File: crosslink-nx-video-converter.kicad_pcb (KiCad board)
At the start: 2 copper layers, 105.7 x 60 mm, 42 parts, among them J1 DC_SOCKET, J2 031-70526-21, J3 031-70526-21, J4 WE_68715014522_ONE-SIDE, J5 FTSH-105-01-F-DV-K, J6 WE_68715014522_ONE-SIDE, J7 2X05, J8 61300411121, Q6 2N7002, SW1 SW_DIP_x06, U10 AP7330-W5-7, U11 LIFCL-40-9BG256C, U12 MT41K128M16JT-125_K, U15 GS2971A, U16 GS2988, U17 SC18IS602BIPW, U18 W25Q32JVSSIQ, U2 LM339, U3 LM339, U4 NCV51200MNTXG, U5 AP62301WU-7, U6 AP62301WU-7, U7 AP62301WU-7, U8 AP7330-W5-7, U9 AP7330-W5-7, Y1 ABM7_27.000MH_D2Y_T, Y2 OSC40M-3.3_S5

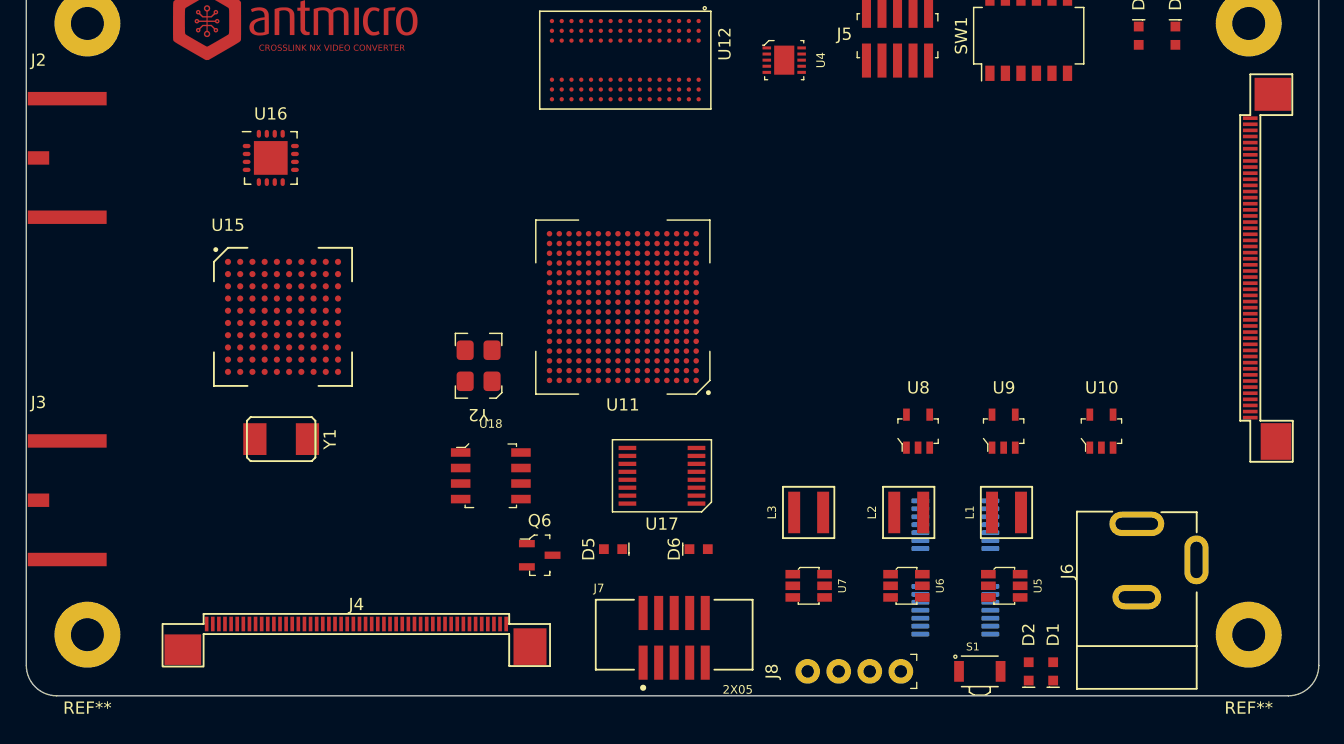
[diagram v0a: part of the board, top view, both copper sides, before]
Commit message: Preliminary FPGA fanout
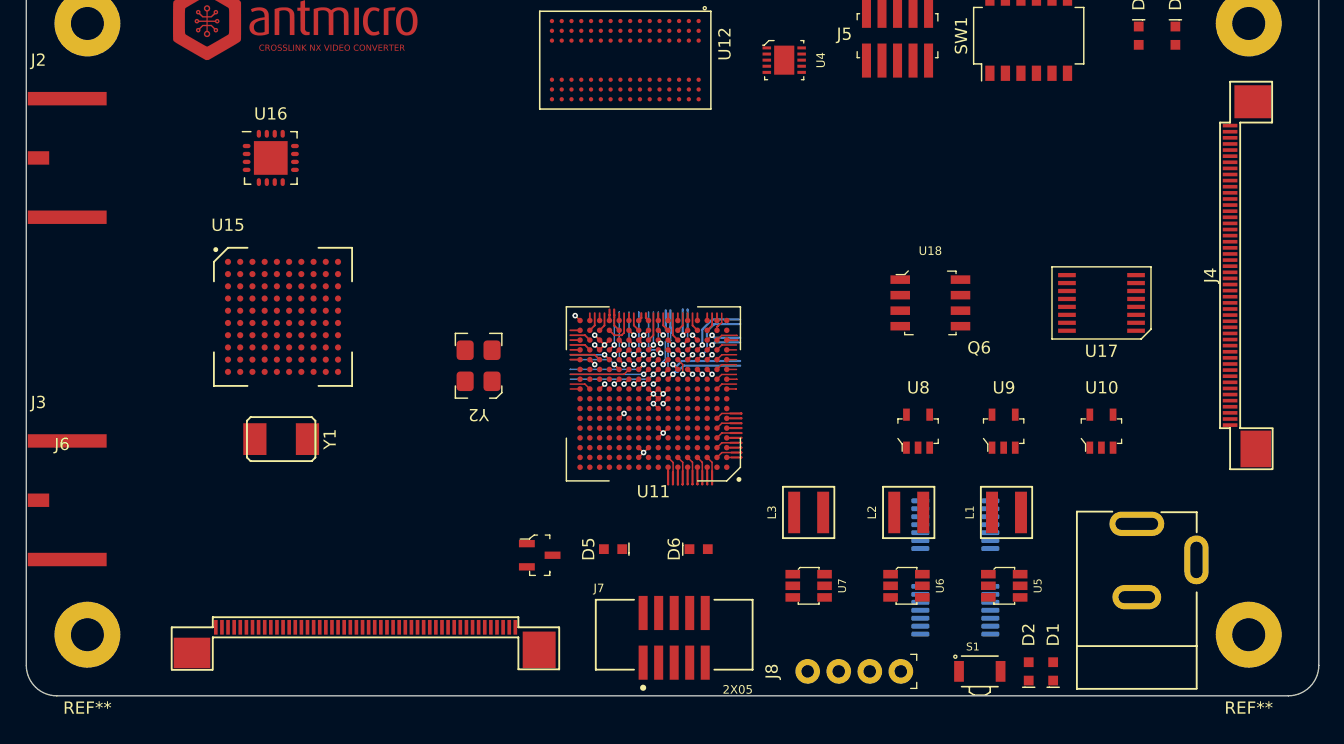
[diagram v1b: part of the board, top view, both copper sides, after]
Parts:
- moved J6 77.3 mm to (102.8, 108.8), turned to 0 degrees
- moved J4 76.2 mm to (172.9, 80.6), turned to 90 degrees
- moved U17 38.6 mm to (163.0, 82.9)
- moved U18 38.6 mm to (149.0, 82.9)
- moved U11 7.53 mm to (126.3, 90.3)
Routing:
- net GND: track 0.00 -> 20.4 mm, vias 0 -> 23
- net /DDR3/DDR3_BA2: track 0.00 -> 7.53 mm, vias 0 -> 1
- net /DDR3/DDR3_A8: track 0.00 -> 6.73 mm, vias 0 -> 1
- net /DDR3/~{DDR3_RAS}: track 0.00 -> 6.57 mm, vias 0 -> 1
- net /Peripherals/MIPI2_D3_N: track 0.00 -> 6.36 mm, vias 0 -> 1
- net /Peripherals/MIPI2_D3_P: track 0.00 -> 6.36 mm, vias 0 -> 1
- net /Peripherals/MIPI2_D2_P: track 0.00 -> 6.19 mm, vias 0 -> 1
- net /Peripherals/MIPI2_D1_N: track 0.00 -> 5.62 mm, vias 0 -> 1
- net /Peripherals/MIPI2_D1_P: track 0.00 -> 5.27 mm, vias 0 -> 1
- net /Peripherals/MIPI2_D2_N: track 0.00 -> 5.24 mm, vias 0 -> 1
- net /DDR3/DDR3_A6: track 0.00 -> 5.03 mm, vias 0 -> 1
- net /DDR3/DDR3_A7: track 0.00 -> 4.97 mm
- net /DDR3/~{DDR3_CAS}: track 0.00 -> 4.42 mm, vias 0 -> 1
- net /DDR3/DDR3_A10: track 0.00 -> 4.33 mm, vias 0 -> 1
- net /DDR3/DDR3_ODT: track 0.00 -> 4.23 mm, vias 0 -> 1
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- added copper zone on In1.Cu, net GND
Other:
- copper layers 2 -> 6

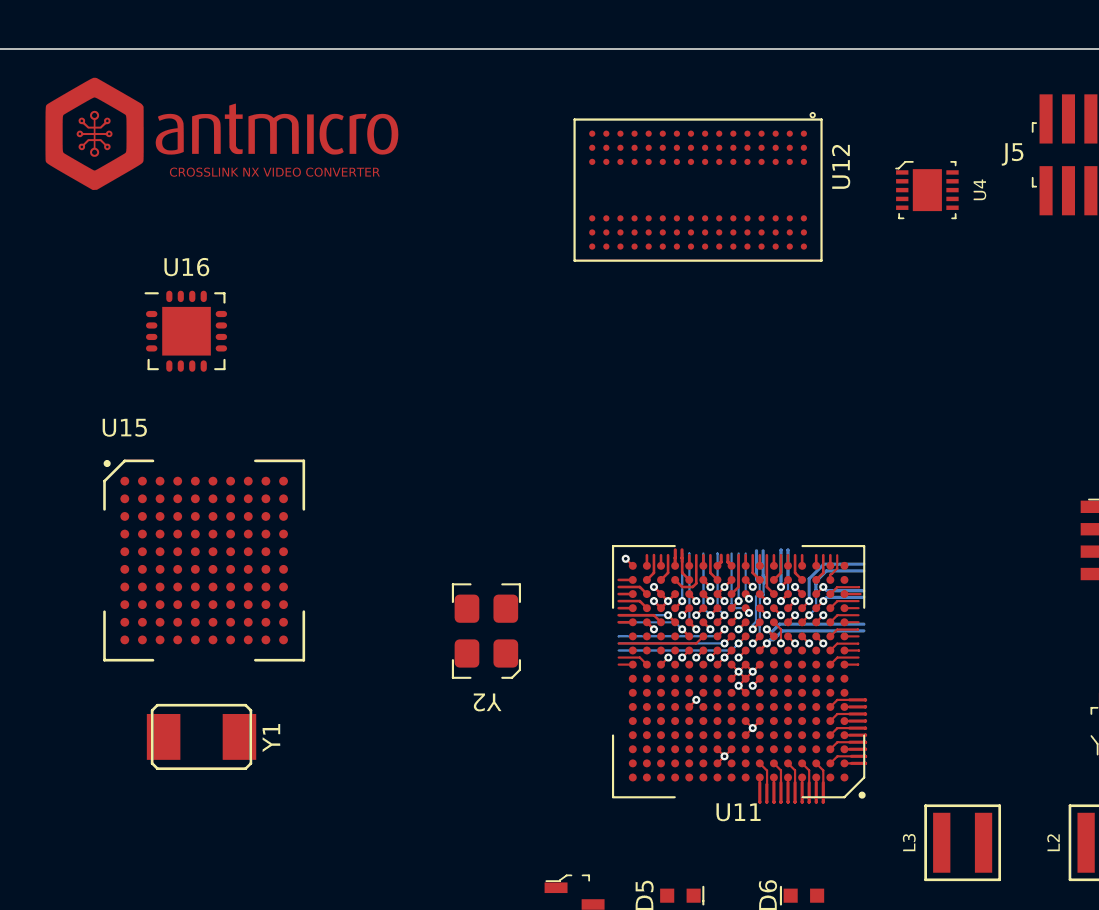
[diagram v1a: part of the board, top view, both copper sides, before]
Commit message: More fanout
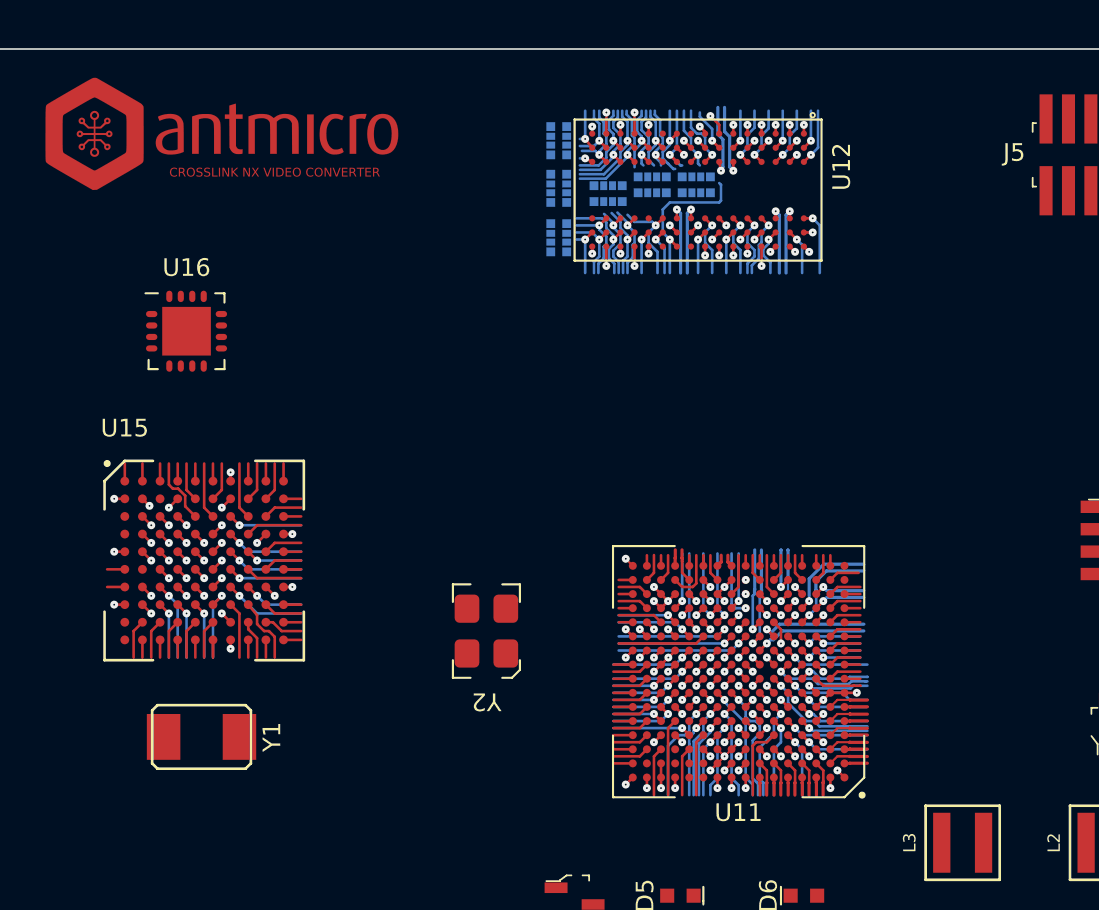
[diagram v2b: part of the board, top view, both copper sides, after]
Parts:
- removed U4: NCV51200MNTXG, crosslink-nx-video-converter-footprints:DFN-10-1EP_3x3mm
- added R44: 4x51R_0402_array, crosslink-nx-video-converter-footprints:R_Array_4x0402, B.Cu at (121.4, 62.7)
- added R45: 4x51R_0402_array, crosslink-nx-video-converter-footprints:R_Array_4x0402, B.Cu at (116.1, 60.2)
- added R46: 4x51R_0402_array, crosslink-nx-video-converter-footprints:R_Array_4x0402, B.Cu at (118.9, 63.2)
- added R48: 4x51R_0402_array, crosslink-nx-video-converter-footprints:R_Array_4x0402, B.Cu at (116.1, 65.7)
- added R49: 4x51R_0402_array, crosslink-nx-video-converter-footprints:R_Array_4x0402, B.Cu at (116.1, 62.9)
- added R50: 4x51R_0402_array, crosslink-nx-video-converter-footprints:R_Array_4x0402, B.Cu at (123.9, 62.7)
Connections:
- J8 pad 2: SCL -> SDA
- J8 pad 3: SDA -> SCL
- U11 pad A14: unconnected-(U11-PadA14) -> GND
- U11 pad A15: unconnected-(U11-PadA15) -> GND
- U11 pad A9: unconnected-(U11-PadA9) -> GND
- U11 pad B9: unconnected-(U11-PadB9) -> GND
- U11 pad C11: unconnected-(U11-PadC11) -> GND
- U11 pad K13: unconnected-(U11-PadK13) -> GND
- U11 pad K14: unconnected-(U11-PadK14) -> GND
- U11 pad K15: unconnected-(U11-PadK15) -> GND
- U11 pad K16: unconnected-(U11-PadK16) -> GND
- U11 pad L13: unconnected-(U11-PadL13) -> GND
- U11 pad L15: unconnected-(U11-PadL15) -> GND
- U11 pad L16: unconnected-(U11-PadL16) -> GND
- U11 pad N6: +1V35 -> +1V5
- U11 pad P11: +1V35 -> +1V5
- U11 pad P12: +1V35 -> +1V5
- U11 pad R2: +1V35 -> +1V5
- U12 pad A1: +1V35 -> +1V5
- U12 pad A8: +1V35 -> +1V5
- U12 pad B2: +1V35 -> +1V5
- U12 pad C1: +1V35 -> +1V5
- U12 pad C9: +1V35 -> +1V5
- U12 pad D2: +1V35 -> +1V5
- U12 pad D9: +1V35 -> +1V5
- U12 pad E9: +1V35 -> +1V5
- U12 pad F1: +1V35 -> +1V5
- U12 pad G7: +1V35 -> +1V5
- U12 pad H2: +1V35 -> +1V5
- U12 pad H9: +1V35 -> +1V5
- U12 pad K2: +1V35 -> +1V5
- U12 pad K8: +1V35 -> +1V5
- U12 pad N1: +1V35 -> +1V5
- U12 pad N9: +1V35 -> +1V5
- U12 pad R1: +1V35 -> +1V5
- U12 pad R9: +1V35 -> +1V5
- U2 pad 10: +1V8 -> /Power Supply/VREF_0V45
- U2 pad 11: /Power Supply/VREF_0V45 -> +1V8
- U2 pad 4: +3V3 -> /Power Supply/VREF_0V45
- U2 pad 5: /Power Supply/VREF_0V45 -> +3V3
- U2 pad 6: 1V0_Power -> /Power Supply/VREF_0V45
- U2 pad 7: /Power Supply/VREF_0V45 -> 1V0_Power
- U2 pad 8: 1V0_Clean -> /Power Supply/VREF_0V45
- U2 pad 9: /Power Supply/VREF_0V45 -> 1V0_Clean
- U3 pad 10: +5V -> GND
- U3 pad 11: /Power Supply/VREF_0V45 -> +5V
- U3 pad 4: +1V35 -> /Power Supply/VREF_0V45
- U3 pad 5: /Power Supply/VREF_0V45 -> +1V5
- U3 pad 6: +1V2 -> /Power Supply/VREF_0V45
- U3 pad 7: /Power Supply/VREF_0V45 -> +1V2
- U3 pad 8: /Power Supply/Vtt_PGOOD -> /Power Supply/VREF_0V45
- U3 pad 9: /Power Supply/VREF_0V45 -> Vtt
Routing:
- net GND: track 20.4 -> 63.0 mm, vias 23 -> 98
- net +1V5: track 0.00 -> 15.9 mm, vias 0 -> 21
- net /SDI/AUDIO_EN/~{DIS}: track 0.00 -> 9.28 mm, vias 0 -> 2
- net /SDI/SDIN_TDI: track 0.00 -> 8.95 mm, vias 0 -> 2
- net /DDR3/DDR3_CKE: track 2.37 -> 11.2 mm, vias 0 -> 1
- net /SDI/SW_EN: track 0.00 -> 8.66 mm, vias 0 -> 1
- net /SDI/SDO_EN/DIS: track 0.00 -> 8.64 mm, vias 0 -> 1
- net /SDI/~{RC_BYP}: track 0.57 -> 9.05 mm, vias 1 -> 2
- net /SDI/SDOUT_TDO: track 0.00 -> 8.45 mm, vias 0 -> 2
- net /SDI/IOPROC_EN/~{DIS}: track 0.00 -> 8.39 mm, vias 0 -> 1
- net /SDI/RESET_TRST: track 0.00 -> 8.24 mm, vias 0 -> 2
- net /SDI/DVB_ASI: track 0.00 -> 8.19 mm, vias 0 -> 2
- net /SDI/JTAG/~{HOST}: track 0.57 -> 8.73 mm
- net /SDI/~{CS_TMS}: track 0.00 -> 8.13 mm, vias 0 -> 2
- net /SDI/SCLK_TCK: track 0.00 -> 8.04 mm, vias 0 -> 1
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
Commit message: Placed components
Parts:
- added C1: C_100n_0402, antmicro-footprints:0402-cap, B.Cu at (144.2, 118.1)
- added C10: C_10u_0603, crosslink-nx-video-converter-footprints:0603-cap, F.Cu at (153.7, 106.7)
- added C100: C_100n_0402, antmicro-footprints:0402-cap, B.Cu at (134.9, 90.5)
- added C101: C_100n_0402, antmicro-footprints:0402-cap, B.Cu at (129.7, 99.4)
- added C102: C_100n_0402, antmicro-footprints:0402-cap, B.Cu at (134.5, 94.5)
- added C103: C_100n_0402, antmicro-footprints:0402-cap, B.Cu at (132.9, 98.2)
- added C104: C_100n_0402, antmicro-footprints:0402-cap, B.Cu at (126.5, 98.8)
- added C105: C_100n_0402, antmicro-footprints:0402-cap, B.Cu at (127.8, 82.1)
- added C106: C_100n_0402, antmicro-footprints:0402-cap, B.Cu at (126.8, 82.1)
- added C107: C_100n_0402, antmicro-footprints:0402-cap, B.Cu at (125.8, 82.1)
- added C11: C_10u_0603, crosslink-nx-video-converter-footprints:0603-cap, F.Cu at (155.1, 99.1)
- added C12: C_10u_0603, crosslink-nx-video-converter-footprints:0603-cap, F.Cu at (164.4, 104.8)
- added C13: C_10u_0603, crosslink-nx-video-converter-footprints:0603-cap, F.Cu at (154.6, 110.2)
- added C14: C_100n_0402, antmicro-footprints:0402-cap, F.Cu at (166.7, 99.8)
- added C15: C_100n_0402, antmicro-footprints:0402-cap, F.Cu at (149.5, 107.9)
- added C16: C_100n_0402, antmicro-footprints:0402-cap, B.Cu at (118.2, 83.0)
- added C17: C_1u_0603, crosslink-nx-video-converter-footprints:0603-cap, F.Cu at (142.7, 114.0)
- added C18: C_1u_0603, crosslink-nx-video-converter-footprints:0603-cap, F.Cu at (135.5, 114.8)
- added C19: C_1u_0603, crosslink-nx-video-converter-footprints:0603-cap, F.Cu at (139.3, 113.5)
- added C2: C_100n_0402, antmicro-footprints:0402-cap, B.Cu at (138.0, 111.2)
- added C20: C_22u_0603, antmicro-footprints:0603-cap, F.Cu at (149.8, 102.5)
- added C21: C_22u_0603, antmicro-footprints:0603-cap, F.Cu at (161.0, 99.5)
- added C22: C_22u_0603, antmicro-footprints:0603-cap, F.Cu at (149.2, 113.6)
- added C23: C_22u_0603, antmicro-footprints:0603-cap, F.Cu at (149.8, 104.1)
- added C24: C_22u_0603, antmicro-footprints:0603-cap, F.Cu at (159.4, 99.5)
- added C25: C_22u_0603, antmicro-footprints:0603-cap, F.Cu at (149.2, 115.2)
- added C26: C_22u_0603, antmicro-footprints:0603-cap, F.Cu at (152.3, 102.5)
- added C27: C_22u_0603, antmicro-footprints:0603-cap, F.Cu at (161.0, 102.1)
- added C28: C_22u_0603, antmicro-footprints:0603-cap, F.Cu at (151.8, 115.2)
- added C29: C_1u_0603, crosslink-nx-video-converter-footprints:0603-cap, F.Cu at (144.2, 106.6)
- added C3: C_100n_0402, antmicro-footprints:0402-cap, F.Cu at (149.8, 71.1)
- added C30: C_1u_0603, crosslink-nx-video-converter-footprints:0603-cap, F.Cu at (134.0, 106.8)
- added C31: C_10u_0603, crosslink-nx-video-converter-footprints:0603-cap, F.Cu at (137.8, 105.5)
- added C32: C_22u_0603, antmicro-footprints:0603-cap, F.Cu at (152.3, 104.1)
- added C33: C_22u_0603, antmicro-footprints:0603-cap, F.Cu at (159.4, 102.1)
- added C34: C_22u_0603, antmicro-footprints:0603-cap, F.Cu at (151.8, 113.6)
- added C35: C_100n_0402, antmicro-footprints:0402-cap, B.Cu at (134.4, 82.8)
- added C36: C_100n_0402, antmicro-footprints:0402-cap, F.Cu at (121.0, 37.1)
- added C37: C_100n_0402, antmicro-footprints:0402-cap, F.Cu at (128.1, 37.1)
- added C38: C_100n_0402, antmicro-footprints:0402-cap, F.Cu at (121.0, 39.6)
- added C39: C_100n_0402, antmicro-footprints:0402-cap, F.Cu at (124.5, 39.6)
- added C4: C_1u_0603, crosslink-nx-video-converter-footprints:0603-cap, F.Cu at (147.1, 68.8)
- added C40: C_100n_0402, antmicro-footprints:0402-cap, F.Cu at (135.3, 89.0)
- added C41: C_100n_0402, crosslink-nx-video-converter-footprints:0402-cap, F.Cu at (133.6, 38.9)
- added C42: C_100n_0402, crosslink-nx-video-converter-footprints:0402-cap, F.Cu at (120.6, 44.3)
- added C43: C_100n_0402, crosslink-nx-video-converter-footprints:0402-cap, F.Cu at (134.2, 36.9)
- added C44: C_100n_0402, crosslink-nx-video-converter-footprints:0402-cap, F.Cu at (130.0, 41.3)
- added C45: C_100n_0402, crosslink-nx-video-converter-footprints:0402-cap, F.Cu at (127.7, 39.4)
- added C46: C_100n_0402, crosslink-nx-video-converter-footprints:0402-cap, F.Cu at (124.2, 41.8)
- added C47: C_100n_0402, crosslink-nx-video-converter-footprints:0402-cap, F.Cu at (124.2, 43.8)
- added C48: C_100n_0402, crosslink-nx-video-converter-footprints:0402-cap, F.Cu at (130.6, 39.4)
- added C49: C_100n_0402, crosslink-nx-video-converter-footprints:0402-cap, F.Cu at (131.3, 36.9)
- added C5: C_22u_0603, antmicro-footprints:0603-cap, F.Cu at (144.9, 74.0)
- added C50: C_100n_0402, crosslink-nx-video-converter-footprints:0402-cap, F.Cu at (127.1, 43.8)
- added C51: C_33p_0402, antmicro-footprints:0402-cap, F.Cu at (100.4, 87.8)
- added C52: C_33p_0402, antmicro-footprints:0402-cap, F.Cu at (92.8, 87.8)
- added C53: C_1u_0402, crosslink-nx-video-converter-footprints:0402-cap, F.Cu at (79.3, 38.8)
- added C54: C_1u_0402, crosslink-nx-video-converter-footprints:0402-cap, F.Cu at (75.8, 43.3)
- added C55: C_47n_0603, crosslink-nx-video-converter-footprints:0603-cap, F.Cu at (65.4, 34.1)
- added C56: C_470n_0603, crosslink-nx-video-converter-footprints:0603-cap, F.Cu at (61.9, 34.1)
- added C57: C_1u_0402, crosslink-nx-video-converter-footprints:0402-cap, F.Cu at (82.9, 33.9)
- added C58: C_100n_0402, antmicro-footprints:0402-cap, B.Cu at (117.8, 94.8)
- added C59: C_470n_0603, crosslink-nx-video-converter-footprints:0603-cap, F.Cu at (76.1, 34.1)
- added C6: C_100n_0402, antmicro-footprints:0402-cap, F.Cu at (147.2, 73.7)
- added C60: C_100n_0402, antmicro-footprints:0402-cap, F.Cu at (69.0, 39.1)
- added C61: C_100n_0402, antmicro-footprints:0402-cap, F.Cu at (65.4, 39.1)
- added C62: C_100n_0402, antmicro-footprints:0402-cap, F.Cu at (61.9, 41.5)
- added C63: C_100n_0402, antmicro-footprints:0402-cap, F.Cu at (79.6, 34.1)
- added C64: C_100n_0402, antmicro-footprints:0402-cap, F.Cu at (69.0, 44.0)
- added C65: C_100n_0402, antmicro-footprints:0402-cap, B.Cu at (117.8, 93.8)
- added C66: C_100n_0402, antmicro-footprints:0402-cap, F.Cu at (65.4, 36.6)
- added C67: C_100n_0402, antmicro-footprints:0402-cap, F.Cu at (61.9, 44.0)
- added C68: C_100n_0402, antmicro-footprints:0402-cap, F.Cu at (72.5, 34.1)
- added C69: C_100n_0402, antmicro-footprints:0402-cap, F.Cu at (72.5, 39.1)
- added C7: C_22u_0603, antmicro-footprints:0603-cap, F.Cu at (141.8, 70.3)
- added C70: C_100n_0402, antmicro-footprints:0402-cap, F.Cu at (61.9, 36.6)
- added C71: C_33u_0603, crosslink-nx-video-converter-footprints:0603-cap, F.Cu at (65.4, 46.5)
- added C72: C_100n_0402, antmicro-footprints:0402-cap, F.Cu at (61.9, 46.5)
- added C73: C_100n_0402, antmicro-footprints:0402-cap, F.Cu at (65.4, 44.0)
- added C74: C_100n_0402, antmicro-footprints:0402-cap, F.Cu at (65.4, 41.5)
- added C75: C_100n_0402, antmicro-footprints:0402-cap, F.Cu at (69.0, 34.1)
- added C76: C_10n_0402, crosslink-nx-video-converter-footprints:0402-cap, F.Cu at (68.7, 48.2)
- added C77: C_4u7_0402, crosslink-nx-video-converter-footprints:0402-cap, F.Cu at (75.8, 41.3)
- added C78: C_4u7_0402, crosslink-nx-video-converter-footprints:0402-cap, F.Cu at (72.2, 45.8)
- added C79: C_100n_0402, antmicro-footprints:0402-cap, F.Cu at (115.8, 88.8)
- added C8: C_22u_0603, antmicro-footprints:0603-cap, F.Cu at (140.2, 70.3)
- added C80: C_100n_0402, antmicro-footprints:0402-cap, F.Cu at (152.0, 118.0)
- added C81: C_100n_0402, antmicro-footprints:0402-cap, B.Cu at (158.2, 71.2)
- added C82: C_100n_0402, antmicro-footprints:0402-cap, B.Cu at (105.6, 95.2)
- added C83: C_100n_0402, antmicro-footprints:0402-cap, B.Cu at (135.1, 86.9)
- added C84: C_100n_0402, antmicro-footprints:0402-cap, F.Cu at (135.3, 88.0)
- added C85: C_100n_0402, antmicro-footprints:0402-cap, B.Cu at (124.5, 98.8)
- added C86: C_10u_0603, crosslink-nx-video-converter-footprints:0603-cap, F.Cu at (214.2, 111.4)
- added C87: C_10u_0603, crosslink-nx-video-converter-footprints:0603-cap, F.Cu at (200.0, 111.4)
- added C88: C_10u_0603, crosslink-nx-video-converter-footprints:0603-cap, F.Cu at (200.0, 118.8)
- added C89: C_10u_0603, crosslink-nx-video-converter-footprints:0603-cap, F.Cu at (207.1, 113.9)
- added C9: C_100n_0402, antmicro-footprints:0402-cap, F.Cu at (150.1, 96.8)
- added C90: C_10u_0603, crosslink-nx-video-converter-footprints:0603-cap, F.Cu at (203.6, 118.8)
- added C91: C_1u_0603, crosslink-nx-video-converter-footprints:0603-cap, F.Cu at (217.8, 113.9)
- added C92: C_10u_0603, crosslink-nx-video-converter-footprints:0603-cap, F.Cu at (203.6, 121.3)
- added C93: C_100n_0402, antmicro-footprints:0402-cap, B.Cu at (129.8, 82.1)
- added C94: C_100n_0402, antmicro-footprints:0402-cap, B.Cu at (134.9, 91.5)
- added C95: C_100n_0402, antmicro-footprints:0402-cap, B.Cu at (127.5, 99.5)
- added C96: C_100n_0402, antmicro-footprints:0402-cap, B.Cu at (134.5, 96.3)
- added C97: C_100n_0402, antmicro-footprints:0402-cap, B.Cu at (134.0, 98.2)
- added C98: C_100n_0402, antmicro-footprints:0402-cap, B.Cu at (125.5, 98.8)
- added C99: C_100n_0402, antmicro-footprints:0402-cap, B.Cu at (128.8, 82.1)
- added F1: 04671.25NR, crosslink-nx-video-converter-footprints:0603-Fuse-Littelfuse-0467, F.Cu at (171.6, 67.7)
- added F2: 04671.25NR, crosslink-nx-video-converter-footprints:0603-Fuse-Littelfuse-0467, F.Cu at (169.8, 67.7)
- added FB1: BLM18PG121SN1D, crosslink-nx-video-converter-footprints:0603-res, F.Cu at (217.8, 116.3)
- added FB2: BLM18PG121SN1D, crosslink-nx-video-converter-footprints:0603-res, F.Cu at (214.2, 118.8)
- added FB3: BLM18PG121SN1D, crosslink-nx-video-converter-footprints:0603-res, F.Cu at (214.2, 113.9)
- added FB4: BLM18PG121SN1D, crosslink-nx-video-converter-footprints:0603-res, F.Cu at (203.6, 111.4)
- added FB5: BLM18PG121SN1D, crosslink-nx-video-converter-footprints:0603-res, F.Cu at (207.1, 121.3)
- added L4: L_0402_6n2, crosslink-nx-video-converter-footprints:0402-cap, F.Cu at (85.8, 33.9)
- added L5: L_0402_6n2, crosslink-nx-video-converter-footprints:0402-cap, F.Cu at (75.1, 45.3)
- added Q1: 2N7002, crosslink-nx-video-converter-footprints:SOT-23-3, B.Cu at (161.3, 112.4)
- added Q2: AO3401A, crosslink-nx-video-converter-footprints:SOT-23-3, B.Cu at (161.4, 108.3)
- added Q3: AO3401A, crosslink-nx-video-converter-footprints:SOT-23-3, B.Cu at (154.3, 119.2)
- added Q4: 2N7002, crosslink-nx-video-converter-footprints:SOT-23-3, B.Cu at (153.2, 115.2)
- added Q5: AO3401A, crosslink-nx-video-converter-footprints:SOT-23-3, B.Cu at (158.1, 117.3)
- added R1: R_100k_0402, antmicro-footprints:0402-res, F.Cu at (149.8, 72.1)
- added R10: R_1k3_0402, antmicro-footprints:0402-res, F.Cu at (166.1, 105.0)
- added R11: R_10k_0402, antmicro-footprints:0402-res, B.Cu at (155.7, 116.2)
- added R12: R_1k5_0402, antmicro-footprints:0402-res, F.Cu at (166.1, 104.0)
- added R13: R_0R_0805, crosslink-nx-video-converter-footprints:0805-res, B.Cu at (157.3, 113.0)
- added R14: R_470R_0402, antmicro-footprints:0402-res, F.Cu at (159.0, 117.6)
- added R15: R_0R_0805, crosslink-nx-video-converter-footprints:0805-res, F.Cu at (154.8, 101.8)
- added R16: R_0R_0805, crosslink-nx-video-converter-footprints:0805-res, F.Cu at (161.7, 104.5)
- added R17: R_0R_0805, crosslink-nx-video-converter-footprints:0805-res, F.Cu at (154.2, 112.9)
- added R18: R_470R_0402, antmicro-footprints:0402-res, F.Cu at (157.0, 117.6)
- added R19: R_0R_0402, antmicro-footprints:0402-res, F.Cu at (141.3, 112.6)
- added R2: R_10k_0402, antmicro-footprints:0402-res, B.Cu at (142.0, 118.1)
- added R20: R_0R_0402, antmicro-footprints:0402-res, F.Cu at (133.6, 114.0)
- added R21: R_0R_0402, antmicro-footprints:0402-res, F.Cu at (137.4, 112.6)
- added R22: R_3k01_0402, antmicro-footprints:0402-res, F.Cu at (155.2, 97.3)
- added R23: R_10k_0402, antmicro-footprints:0402-res, F.Cu at (154.2, 97.3)
- added R24: R_0R_0402, antmicro-footprints:0402-res, F.Cu at (142.8, 112.2)
- added R25: R_0R_0402, antmicro-footprints:0402-res, F.Cu at (135.2, 113.5)
- added R26: R_33k_0402, antmicro-footprints:0402-res, F.Cu at (154.8, 108.5)
- added R27: R_10k_0402, antmicro-footprints:0402-res, F.Cu at (153.8, 108.5)
- added R28: R_0R_0402, antmicro-footprints:0402-res, F.Cu at (138.9, 112.2)
- added R29: R_0R_0402, antmicro-footprints:0402-res, F.Cu at (141.9, 106.8)
- added R3: R_1k_0402, antmicro-footprints:0402-res, B.Cu at (139.9, 118.1)
- added R30: R_0R_0402, antmicro-footprints:0402-res, F.Cu at (134.3, 108.1)
- added R31: R_3k01_0402, antmicro-footprints:0402-res, F.Cu at (144.6, 109.0)
- added R32: R_10k_0402, antmicro-footprints:0402-res, F.Cu at (146.1, 107.9)
- added R33: R_12k_0402, antmicro-footprints:0402-res, F.Cu at (132.3, 110.0)
- added R34: R_24k_0402, antmicro-footprints:0402-res, F.Cu at (136.1, 107.7)
- added R35: R_18k7_1%_0603, crosslink-nx-video-converter-footprints:0603-res, F.Cu at (144.5, 164.0)
- added R36: R_15k_0603, crosslink-nx-video-converter-footprints:0603-res, F.Cu at (133.8, 159.5)
- added R37: R_0R_0402, antmicro-footprints:0402-res, F.Cu at (138.1, 106.8)
- added R38: R_0R_0402, antmicro-footprints:0402-res, F.Cu at (92.3, 93.8)
- added R39: R_0R_0402, antmicro-footprints:0402-res, F.Cu at (113.4, 85.6)
- added R4: R_0R_0805, crosslink-nx-video-converter-footprints:0805-res, F.Cu at (116.2, 114.4)
- added R40: R_0R_0805, crosslink-nx-video-converter-footprints:0805-res, F.Cu at (145.9, 113.8)
- added R41: R_0R_0805, crosslink-nx-video-converter-footprints:0805-res, F.Cu at (146.5, 102.7)
- added R42: R_0R_0805, crosslink-nx-video-converter-footprints:0805-res, F.Cu at (160.8, 96.2)
- added R43: R_100R_0402, crosslink-nx-video-converter-footprints:0402-res, F.Cu at (130.0, 43.3)
- added R47: R_240R_1%_0402, crosslink-nx-video-converter-footprints:0402-res, F.Cu at (127.1, 41.8)
- added R5: R_0R_0805, crosslink-nx-video-converter-footprints:0805-res, F.Cu at (148.1, 75.2)
- added R51: R_75R_0402, crosslink-nx-video-converter-footprints:0402-res, F.Cu at (71.6, 47.7)
- added R52: R_75R_0402, crosslink-nx-video-converter-footprints:0402-res, F.Cu at (68.7, 46.2)
- added R53: R_37R4_0402, crosslink-nx-video-converter-footprints:0402-res, F.Cu at (85.8, 35.9)
- added R54: R_100k_0402, antmicro-footprints:0402-res, F.Cu at (93.2, 71.2)
- added R55: R_100k_0402, antmicro-footprints:0402-res, F.Cu at (76.1, 36.6)
- added R56: R_105R_0402, crosslink-nx-video-converter-footprints:0402-res, F.Cu at (78.7, 43.3)
- added R57: R_750R_0603, crosslink-nx-video-converter-footprints:0603-res, F.Cu at (69.0, 41.5)
- added R58: R_0R_0402, antmicro-footprints:0402-res, F.Cu at (166.0, 69.8)
- added R59: R_75R_0402, crosslink-nx-video-converter-footprints:0402-res, F.Cu at (78.7, 41.3)
- added R6: R_0R_0805, crosslink-nx-video-converter-footprints:0805-res, F.Cu at (150.9, 69.6)
- added R60: R_75R_0402, crosslink-nx-video-converter-footprints:0402-res, F.Cu at (72.2, 43.8)
- added R61: R_75R_0402, crosslink-nx-video-converter-footprints:0402-res, F.Cu at (82.9, 35.9)
- added R62: R_75R_0402, crosslink-nx-video-converter-footprints:0402-res, F.Cu at (82.2, 38.8)
- added R63: R_470R_0402, antmicro-footprints:0402-res, F.Cu at (124.9, 50.1)
- added R64: R_470R_0402, antmicro-footprints:0402-res, F.Cu at (128.4, 50.1)
- added R65: R_0R_0402, antmicro-footprints:0402-res, F.Cu at (166.0, 68.8)
- added R66: R_0R_0402, antmicro-footprints:0402-res, F.Cu at (166.0, 72.4)
- added R67: R_0R_0402, antmicro-footprints:0402-res, F.Cu at (150.0, 118.0)
- added R68: R_10k_0402, antmicro-footprints:0402-res, F.Cu at (150.0, 119.5)
- added R69: R_0R_0402, antmicro-footprints:0402-res, B.Cu at (106.3, 97.3)
- added R7: R_100k_0402, antmicro-footprints:0402-res, B.Cu at (163.9, 111.7)
- added R70: R_100R_0402, antmicro-footprints:0402-res, F.Cu at (155.5, 117.5)
- added R71: R_0R_0402, antmicro-footprints:0402-res, B.Cu at (102.6, 94.0)
- added R72: R_100R_0402, antmicro-footprints:0402-res, F.Cu at (154.0, 118.0)
- added R73: R_0R_0402, antmicro-footprints:0402-res, B.Cu at (102.6, 96.3)
- added R74: R_0R_0402, antmicro-footprints:0402-res, B.Cu at (108.3, 93.9)
- added R75: R_0R_0402, antmicro-footprints:0402-res, B.Cu at (108.2, 96.3)
- added R76: R_0R_0402, antmicro-footprints:0402-res, B.Cu at (104.0, 93.4)
- added R77: R_0R_0402, antmicro-footprints:0402-res, F.Cu at (132.8, 118.4)
- added R78: R_0R_0402, antmicro-footprints:0402-res, F.Cu at (156.0, 74.5)
- added R79: R_1k_0402, antmicro-footprints:0402-res, F.Cu at (156.0, 69.2)
- added R8: R_22R_0402, antmicro-footprints:0402-res, F.Cu at (151.8, 71.1)
- added R80: R_0R_0402, antmicro-footprints:0402-res, F.Cu at (156.0, 73.5)
- added R81: R_10k_0402, antmicro-footprints:0402-res, F.Cu at (131.6, 118.4)
- added R82: R_0R_0402, antmicro-footprints:0402-res, F.Cu at (101.3, 92.9)
- added R83: R_4k7_0402, antmicro-footprints:0402-res, B.Cu at (104.5, 96.7)
- added R84: R_100R_0402, antmicro-footprints:0402-res, F.Cu at (131.6, 120.4)
- added R85: R_0R_0402, antmicro-footprints:0402-res, F.Cu at (156.0, 72.5)
- added R86: R_0R_0402, antmicro-footprints:0402-res, F.Cu at (120.2, 116.6)
- added R87: R_4k7_0402, antmicro-footprints:0402-res, B.Cu at (106.7, 94.9)
- added R88: R_0R_0402, antmicro-footprints:0402-res, F.Cu at (148.0, 65.5)
- added R89: R_2k2_0402, antmicro-footprints:0402-res, F.Cu at (125.9, 116.9)
- added R9: R_10k_0402, antmicro-footprints:0402-res, B.Cu at (161.3, 116.0)
- added R90: R_4k7_0402, antmicro-footprints:0402-res, B.Cu at (105.6, 93.2)
- added R91: R_10k_0402, antmicro-footprints:0402-res, F.Cu at (120.2, 118.6)
- added R92: R_0R_0402, antmicro-footprints:0402-res, F.Cu at (147.0, 65.5)
- added R93: R_2k2_0402, antmicro-footprints:0402-res, F.Cu at (120.2, 120.6)
- added R94: R_0R_0402, antmicro-footprints:0402-res, F.Cu at (146.0, 65.5)
- added R95: R_0R_0402, antmicro-footprints:0402-res, F.Cu at (145.0, 65.5)
- added R96: R_0R_0402, antmicro-footprints:0402-res, F.Cu at (144.0, 65.5)
- added R97: R_10k_0402, antmicro-footprints:0402-res, F.Cu at (143.0, 65.5)
- added TP1: TP_SMD_0_75MM, antmicro-footprints:Testpoint_smd_0_75mm, F.Cu at (129.7, 115.9)
- added TP10: TP_SMD_0_75MM, antmicro-footprints:Testpoint_smd_0_75mm, F.Cu at (151.9, 96.8)
- added TP11: TP_SMD_0_75MM, antmicro-footprints:Testpoint_smd_0_75mm, F.Cu at (166.7, 101.7)
- added TP12: TP_SMD_0_75MM, antmicro-footprints:Testpoint_smd_0_75mm, F.Cu at (151.3, 107.9)
- added TP13: TP_SMD_0_75MM, antmicro-footprints:Testpoint_smd_0_75mm, F.Cu at (95.6, 85.7)
- added TP14: TP_SMD_0_75MM, antmicro-footprints:Testpoint_smd_0_75mm, F.Cu at (81.4, 41.1)
- added TP15: TP_SMD_0_75MM, antmicro-footprints:Testpoint_smd_0_75mm, F.Cu at (109.7, 97.1)
- added TP16: TP_SMD_0_75MM, antmicro-footprints:Testpoint_smd_0_75mm, F.Cu at (101.3, 94.5)
- added TP17: TP_SMD_0_75MM, antmicro-footprints:Testpoint_smd_0_75mm, F.Cu at (101.3, 95.9)
- added TP18: TP_SMD_0_75MM, antmicro-footprints:Testpoint_smd_0_75mm, F.Cu at (109.7, 94.6)
- added TP19: TP_SMD_0_75MM, antmicro-footprints:Testpoint_smd_0_75mm, F.Cu at (132.8, 120.0)
- added TP2: TP_SMD_0_75MM, antmicro-footprints:Testpoint_smd_0_75mm, F.Cu at (159.2, 104.2)
- added TP20: TP_SMD_0_75MM, antmicro-footprints:Testpoint_smd_0_75mm, F.Cu at (109.7, 95.8)
- added TP21: TP_SMD_0_75MM, antmicro-footprints:Testpoint_smd_0_75mm, F.Cu at (102.5, 92.0)
- added TP22: TP_SMD_0_75MM, antmicro-footprints:Testpoint_smd_0_75mm, F.Cu at (123.4, 117.5)
- added TP3: TP_SMD_0_75MM, antmicro-footprints:Testpoint_smd_0_75mm, F.Cu at (144.6, 115.7)
- added TP4: TP_SMD_0_75MM, antmicro-footprints:Testpoint_smd_0_75mm, F.Cu at (147.5, 105.4)
- added TP5: TP_SMD_0_75MM, antmicro-footprints:Testpoint_smd_0_75mm, F.Cu at (142.5, 105.6)
- added TP6: TP_SMD_0_75MM, antmicro-footprints:Testpoint_smd_0_75mm, F.Cu at (139.7, 105.6)
- added TP7: TP_SMD_0_75MM, antmicro-footprints:Testpoint_smd_0_75mm, F.Cu at (158.1, 97.2)
- added TP8: TP_SMD_0_75MM, antmicro-footprints:Testpoint_smd_0_75mm, F.Cu at (135.3, 105.4)
- added TP9: TP_SMD_0_75MM, antmicro-footprints:Testpoint_smd_0_75mm, F.Cu at (131.2, 115.9)
- added U1: MP20073, antmicro-footprints:MSOP-8-1EP_W3mm, F.Cu at (145.7, 71.4)
- moved J7 52.2 mm to (146.0, 61.0), turned to 180 degrees
- moved U18 45.1 mm to (105.6, 95.2)
- moved U10 29.3 mm to (138.5, 109.5)
- moved U9 26.7 mm to (134.7, 110.8)
- moved U16 25.2 mm to (89.1, 95.5), turned to -90 degrees
- moved Q6 20.0 mm to (129.2, 119.4), turned to 180 degrees
- moved U2 19.1 mm to (136.7, 113.7), turned to 90 degrees
- moved D6 18.2 mm to (123.4, 120.0), turned to -90 degrees
- moved R45 17.7 mm to (128.8, 72.6), turned to 90 degrees
- moved U6 17.6 mm to (164.1, 101.7)
- moved D5 17.3 mm to (126.2, 120.0), turned to -90 degrees
- moved U8 17.1 mm to (142.3, 109.5)
- moved L2 17.0 mm to (164.0, 97.6)
- moved R49 14.5 mm to (128.8, 69.9)
- moved L3 13.4 mm to (147.2, 110.6), turned to -90 degrees
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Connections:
- net Net-(C14-Pad2) renamed /Power Supply/1V0_SW
- net Net-(C15-Pad2) renamed /Power Supply/1V5_SW
- net Net-(C16-Pad2) renamed /Power Supply/3V3_SW
- J2 pad 1: Net-(J2-Pad1) -> /SDI/SDI_IN
- J3 pad 1: Net-(C78-Pad2) -> /SDI/SDI_OUT
- L1 pad 2: Net-(C20-Pad1) -> /Power Supply/1V0_OUT
- L2 pad 2: Net-(C21-Pad1) -> /Power Supply/1V5_OUT
- L3 pad 2: Net-(C22-Pad1) -> /Power Supply/3V3_OUT
- U16 pad 11: Net-(L5-Pad2) -> /SDI/SDI_OUT_N
- U16 pad 12: Net-(C77-Pad1) -> /SDI/SDI_OUT_P
- U5 pad 3: Net-(C11-Pad1) -> /Power Supply/1V0_IN
- U6 pad 3: Net-(C12-Pad1) -> /Power Supply/1V5_IN
- U7 pad 3: Net-(C13-Pad1) -> /Power Supply/3V3_IN
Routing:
- net /Peripherals/MIPI2_D2_N: track 5.11 -> 54.7 mm, vias 1 -> 2
- net /Peripherals/MIPI2_D2_P: track 6.08 -> 55.2 mm, vias 1 -> 2
- net /Peripherals/MIPI0_D0_N: track 2.27 -> 49.5 mm, vias 0 -> 2
- net /Peripherals/MIPI0_D0_P: track 1.30 -> 48.5 mm, vias 0 -> 2
- net /Peripherals/MIPI0_D1_N: track 2.27 -> 49.2 mm
- net /Peripherals/MIPI0_D1_P: track 1.31 -> 48.2 mm
- net /Peripherals/MIPI0_CLK_N: track 2.27 -> 49.0 mm
- net /Peripherals/MIPI0_D3_N: track 2.28 -> 49.0 mm
- net /Peripherals/MIPI0_CLK_P: track 1.31 -> 48.0 mm
- net /Peripherals/MIPI0_D3_P: track 1.31 -> 48.0 mm
- net /Peripherals/MIPI0_D2_N: track 2.27 -> 47.5 mm, vias 0 -> 2
- net /Peripherals/MIPI0_D2_P: track 1.30 -> 46.5 mm, vias 0 -> 2
- net /Peripherals/MIPI2_CLK_N: track 1.87 -> 45.8 mm, vias 0 -> 2
- net /Peripherals/MIPI2_CLK_P: track 0.90 -> 44.7 mm, vias 0 -> 2
- net /Peripherals/MIPI2_D3_N: track 6.36 -> 49.7 mm, vias 1 -> 2
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- added copper zone on In3.Cu, net +1V2
- added copper zone on In3.Cu, net +1V5
- added copper zone on F.Cu, net +3V3
- added copper zone on In3.Cu, net +3V3
- added copper zone on F.Cu, net +5V
- added copper zone on In3.Cu, net /FPGA Power/VCC_ADPHY
- added copper zone on In3.Cu, net /FPGA Power/VCC_AUX
- added copper zone on In3.Cu, net /FPGA Power/VCC_AUXA
- added copper zone on In3.Cu, net /FPGA Power/VCC_DPHY
- added copper zone on In3.Cu, net /FPGA Power/VCC_PLLDPHY
- added copper zone on F.Cu, net /Power Supply/1V0_IN
- added copper zone on F.Cu, net /Power Supply/1V0_OUT
- added copper zone on F.Cu, net /Power Supply/1V0_SW
- added copper zone on F.Cu, net /Power Supply/1V5_IN
- added copper zone on F.Cu, net /Power Supply/1V5_OUT
- added copper zone on F.Cu, net /Power Supply/1V5_SW
- added copper zone on F.Cu, net /Power Supply/3V3_IN
- added copper zone on F.Cu, net /Power Supply/3V3_OUT
- added copper zone on F.Cu, net /Power Supply/3V3_SW
- added copper zone on In3.Cu, net 1V0_Power
- added copper zone on F.Cu, net FFC2_5V
- added copper zone on F.Cu, net GND
- added copper zone on In3.Cu, net Vref
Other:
- board size 105.7 x 60 mm -> 105.8 x 68 mm
